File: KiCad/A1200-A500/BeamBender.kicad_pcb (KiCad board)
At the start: 4 copper layers, 50 x 100 mm, 96 parts, among them J1 4-1734742-0, J2 HDMI_A_1.4, J3 STX-3501-3N, J4 Phoenix_Contact, J5 Conn_01x01, J6 Conn_02x06_Odd_Even, U1 LM1117-3.3, U2 GW1NR-UV9LQ144P, U3 ADV7513BSWZ, U4 MCP1702T-1802E_CB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

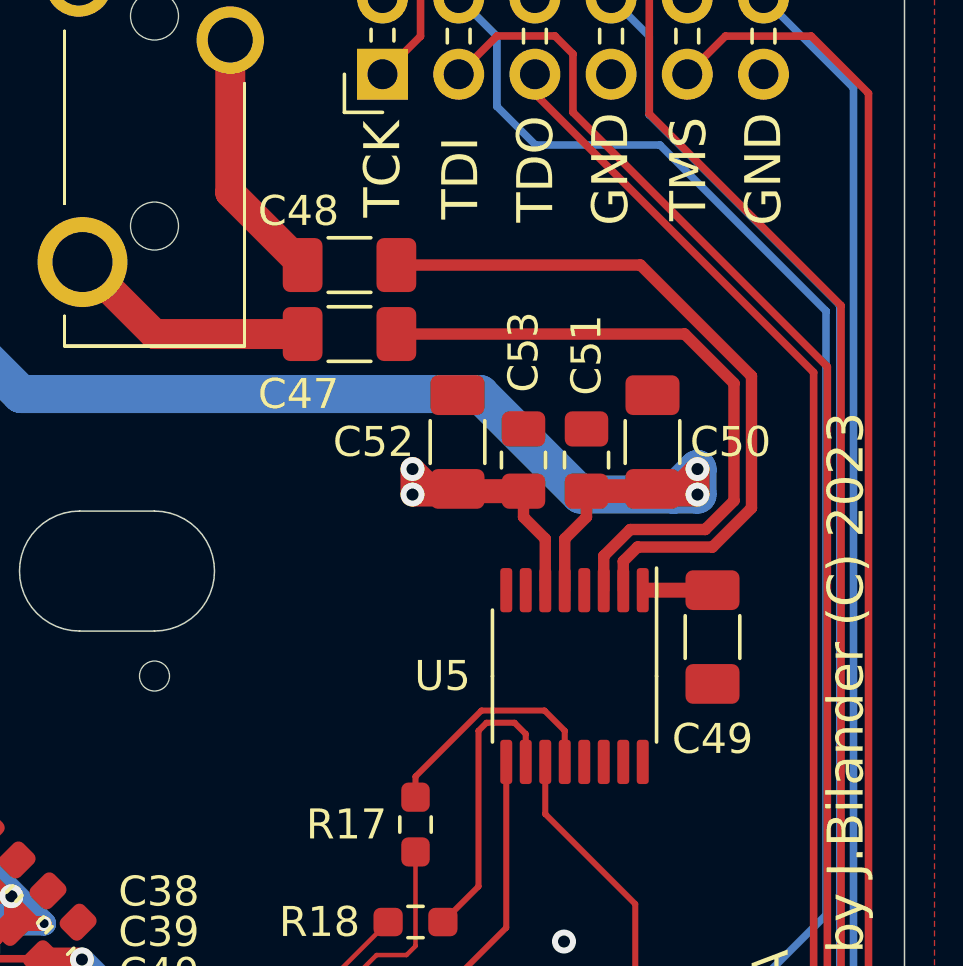
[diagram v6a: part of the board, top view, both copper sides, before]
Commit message: Added a pull-up resistor for GSEL (Gain-Select) input pin with a solder JP to be able to turn gain off = GND
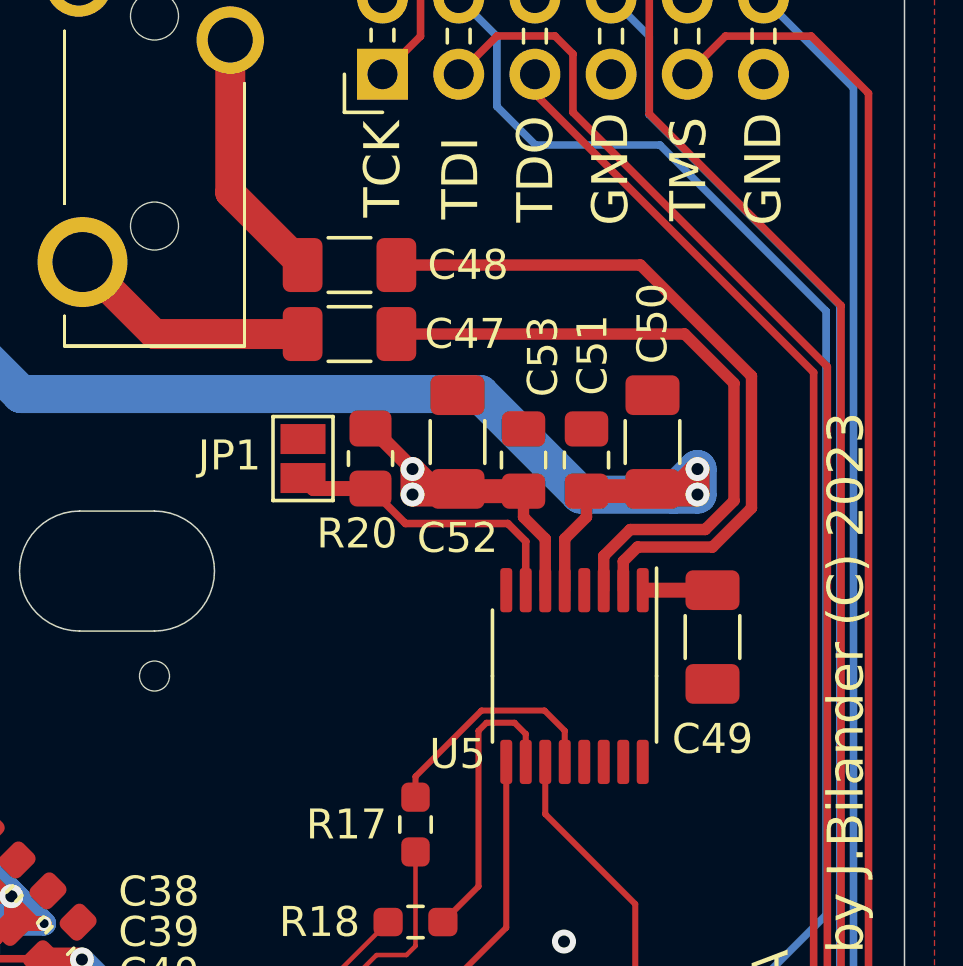
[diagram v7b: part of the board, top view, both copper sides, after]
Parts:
- added JP1: SolderJumper_2_Open, Jumper:SolderJumper-2_P1.3mm_Open_Pad1.0x1.5mm, F.Cu at (128.1, 60.0)
- added R20: 10k, Resistor_SMD:R_0805_2012Metric_Pad1.20x1.40mm_HandSolder, F.Cu at (130.3, 60.0)
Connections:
- U5 pad 7: Net-(U5-Pad7) -> /BeamBender_FPGA/GSEL
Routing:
- net /BeamBender_FPGA/GSEL: track 0.00 -> 9.93 mm
- net 3V3: track 316.3 -> 318.2 mm

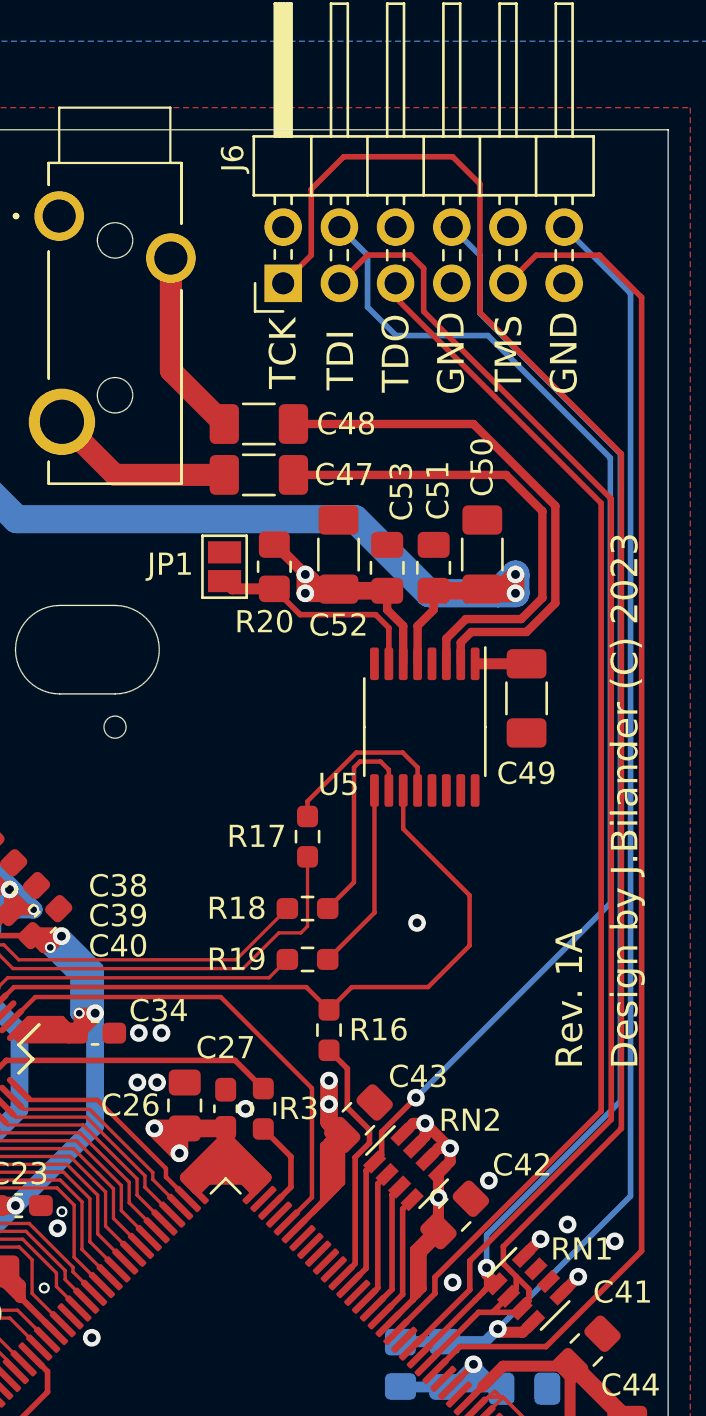
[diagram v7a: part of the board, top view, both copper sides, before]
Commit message: Finished routing the ak5720vt-chip, changed to a potential-divider for controlling GSEL-pin, PDN_RESET,FSEL and DIF-signals routed to spare pins in the FPGA
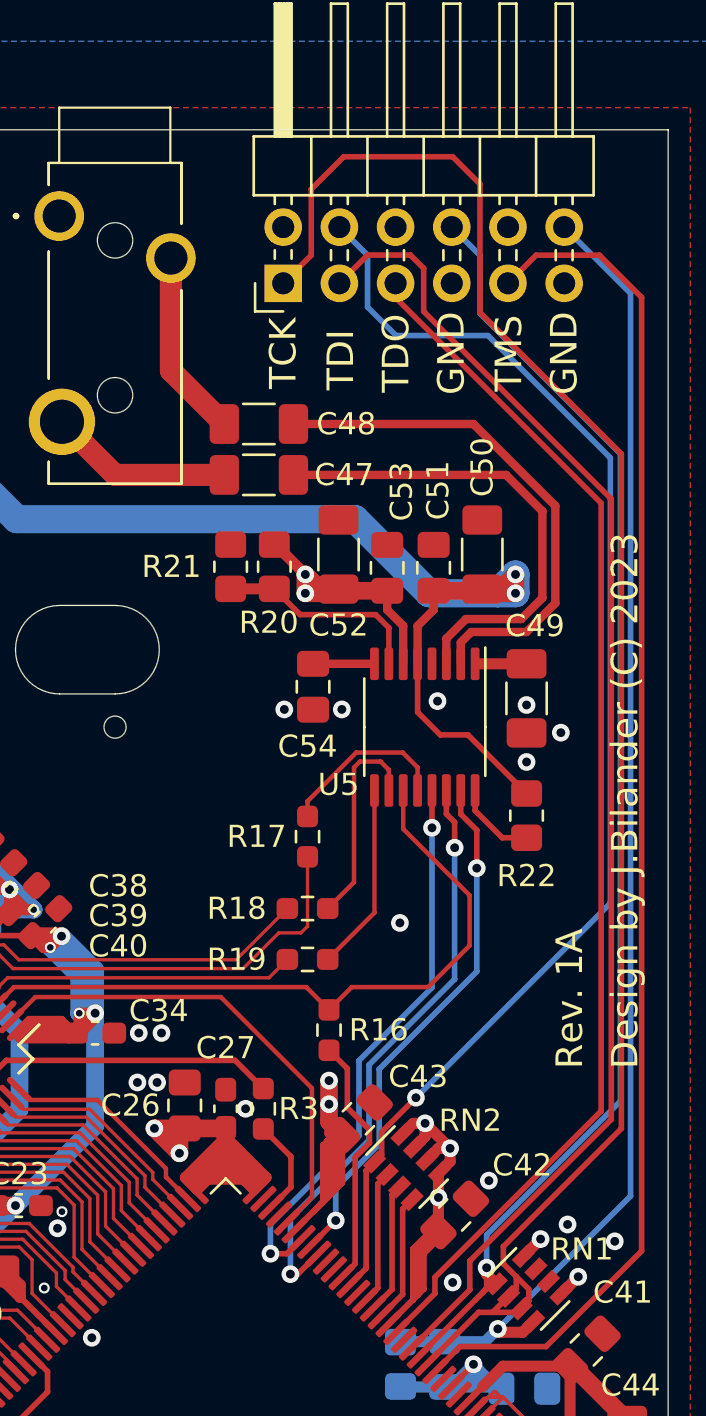
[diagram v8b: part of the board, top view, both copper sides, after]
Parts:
- removed JP1: SolderJumper_2_Open, Jumper:SolderJumper-2_P1.3mm_Open_Pad1.0x1.5mm
- added C54: 1uF (0805), Capacitor_SMD:C_0805_2012Metric_Pad1.18x1.45mm_HandSolder, F.Cu at (132.1, 65.4)
- added R21: 10k, Resistor_SMD:R_0805_2012Metric_Pad1.20x1.40mm_HandSolder, F.Cu at (128.3, 60.0)
- added R22: 0, Resistor_SMD:R_0805_2012Metric_Pad1.20x1.40mm_HandSolder, F.Cu at (141.7, 71.2)
- R20: value 10k -> 1k
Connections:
- net Net-(C47-Pad2) renamed /BeamBender_FPGA/LIN
- net Net-(C48-Pad2) renamed /BeamBender_FPGA/RIN
- net Net-(R17-Pad1) renamed /BeamBender_FPGA/BICK
- net Net-(R18-Pad1) renamed /BeamBender_FPGA/LRCK
- net Net-(R19-Pad1) renamed /BeamBender_FPGA/SDTO
- U2 pad 28: Net-(U2-Pad28) -> DIF|TDMI
- U2 pad 29: Net-(U2-Pad29) -> FSEL
- U2 pad 30: Net-(U2-Pad30) -> PDN_RESET_N
- U5 pad 13: Net-(U5-Pad13) -> PDN_RESET_N
- U5 pad 14: Net-(U5-Pad14) -> DIF|TDMI
- U5 pad 15: Net-(U5-Pad15) -> FSEL
- U5 pad 16: Net-(U5-Pad16) -> /BeamBender_FPGA/CKS
- U5 pad 8: Net-(U5-Pad8) -> /BeamBender_FPGA/REGO
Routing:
- net DIF|TDMI: track 0.00 -> 26.7 mm, vias 0 -> 2
- net PDN_RESET_N: track 0.00 -> 25.7 mm, vias 0 -> 2
- net FSEL: track 0.00 -> 24.0 mm, vias 0 -> 2
- net VCC: track 191.1 -> 199.7 mm
- net /BeamBender_FPGA/CKS: track 0.00 -> 3.74 mm
- net /BeamBender_FPGA/REGO: track 0.00 -> 2.78 mm
- net GND: vias 76 -> 82
